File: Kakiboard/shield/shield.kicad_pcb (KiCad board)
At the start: 2 copper layers, 136.7 x 107.1 mm, 68 parts, among them SW1 SW_Push, SW10 SW_Push, SW11 SW_Push, SW12 SW_Push, SW13 SW_Push, SW14 SW_Push, SW15 SW_Push, SW16 SW_Push, SW17 SW_Push, SW18 SW_Push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

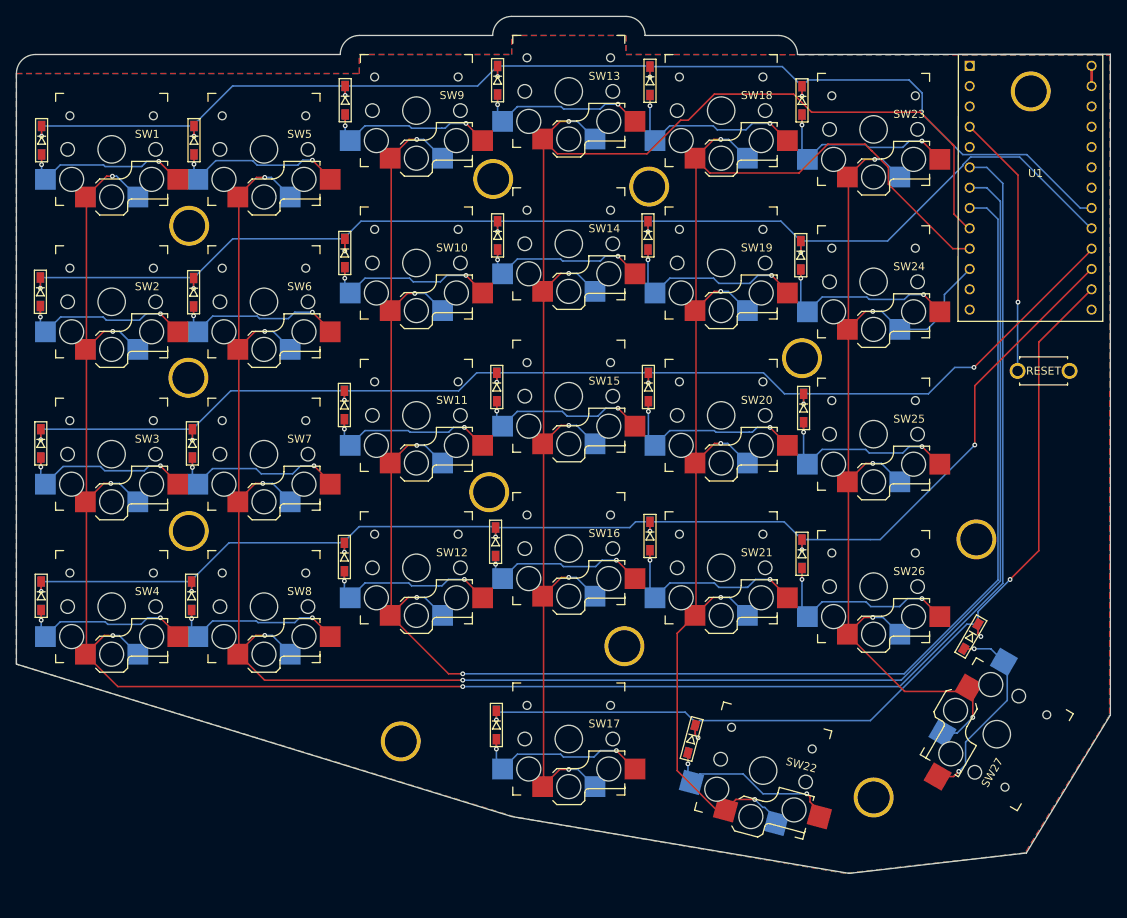
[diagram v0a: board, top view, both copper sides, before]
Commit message: change position for thumb keys
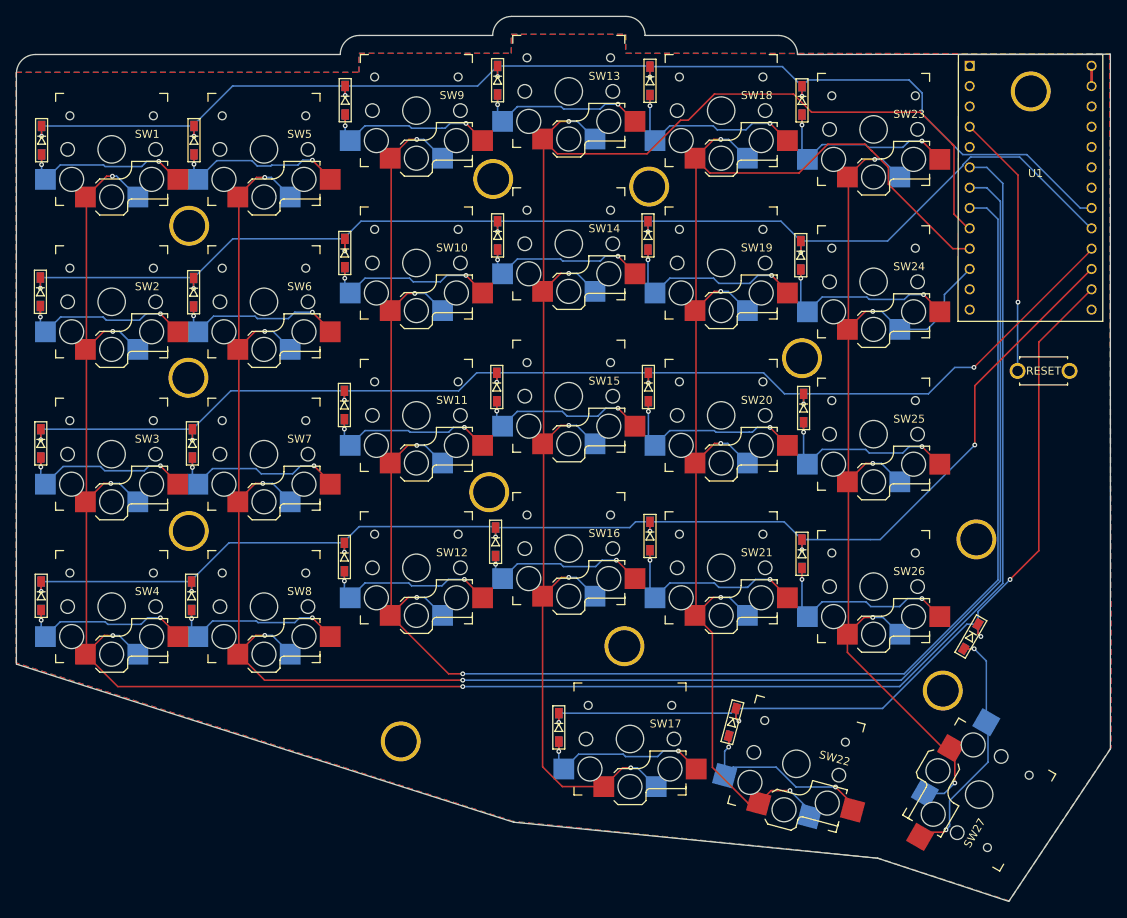
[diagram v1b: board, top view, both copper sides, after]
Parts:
- moved ? 15.9 mm to (192.0, 131.9)
- moved SW27 7.86 mm to (196.6, 144.9)
- moved D17 7.81 mm to (144.0, 136.5)
- moved SW17 7.65 mm to (152.9, 137.9)
- moved D22 5.52 mm to (165.7, 135.8)
- moved SW22 4.24 mm to (173.7, 141.1)
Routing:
- net RO4: track 123.2 -> 113.8 mm
- net CO3: track 192.4 -> 198.8 mm
- net Net-(D27-Pad2): track 26.3 -> 31.7 mm
- net CO5: track 130.8 -> 132.9 mm
- net Net-(D22-Pad2): track 24.7 -> 25.6 mm
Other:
- board size 136.7 x 107.1 mm -> 136.7 x 110.6 mm
